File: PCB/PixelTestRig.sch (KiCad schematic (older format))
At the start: 24 parts, among them J1 RPi_GPIO, J2 GS2, P0 STRIP_OUT, P1 STRIP_OUT, P2 STRIP_OUT, P3 STRIP_OUT, P4 STRIP_OUT, P5 STRIP_OUT, P6 APM_INPUT, Q0 IRLB8721PBF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

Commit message: Completed layout
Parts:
- removed PWR2: 1x02, w_conn_mkds:mkds_1,5-2, symbol CONN_01X02
- added R10, R11, R6, R7, R8, R9: 220R, Resistors_THT:R_Axial_DIN0204_L3.6mm_D1.6mm_P5.08mm_Horizontal, symbol R_Small
- Q0, Q1, Q2, Q3, Q4, Q5: footprint (none) -> TO_SOT_Packages_THT:TO-220-3_Vertical
- R0, R1, R2, R3, R4, R5: footprint (none) -> Resistors_THT:R_Axial_DIN0204_L3.6mm_D1.6mm_P5.08mm_Horizontal
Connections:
- net CTL_0: now also R11.1; no longer Q0.1 (G), R0.1
- net CTL_1: now also R10.1; no longer Q1.1 (G), R1.1
- net CTL_2: now also R9.1; no longer Q2.1 (G), R2.1
- net CTL_3: now also R8.1; no longer Q3.1 (G), R3.1
- net CTL_4: now also R7.1; no longer Q4.1 (G), R4.1
- net CTL_5: now also R6.1; no longer Q5.1 (G), R5.1
- new net: Q3.1 (G), R3.1, R9.2
- new net: Q2.1 (G), R2.1, R8.2
- new net: Q5.1 (G), R11.2, R5.1
- new net: Q4.1 (G), R10.2, R4.1
- new net: Q1.1 (G), R1.1, R7.2
- new net: Q0.1 (G), R0.1, R6.2
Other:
- moved on the sheet: J1, J2, P0, P1, P2, P3, P4, P5, P6, PWR1, Q0, Q1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

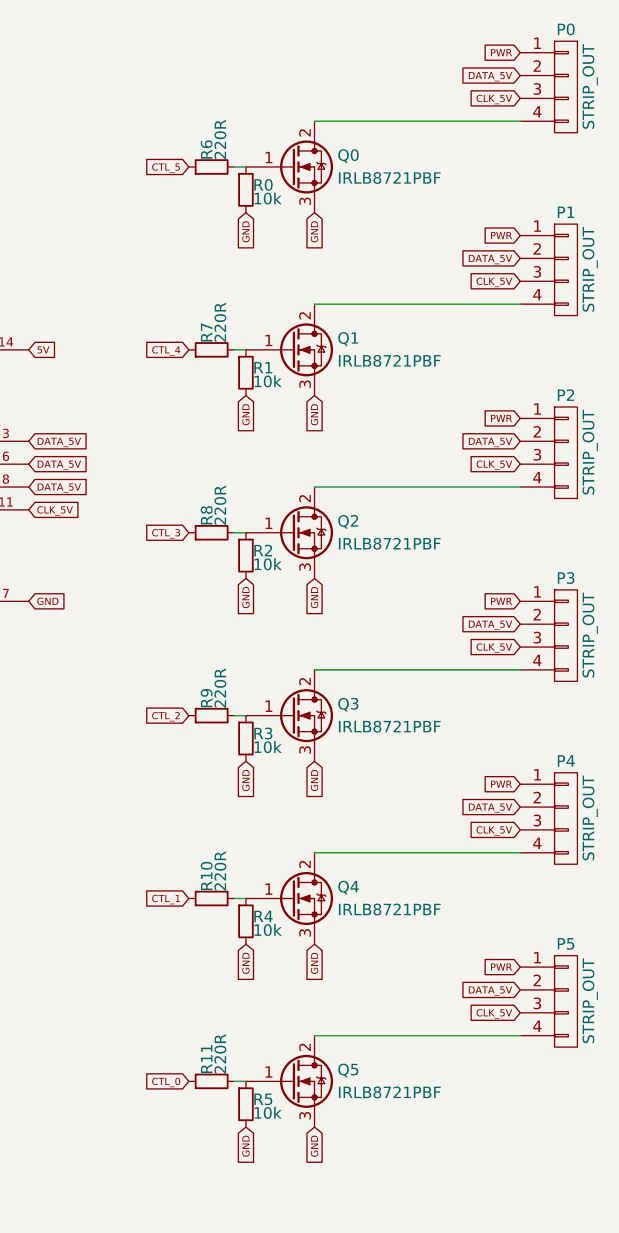
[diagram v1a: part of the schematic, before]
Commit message: Now using PNP transistor
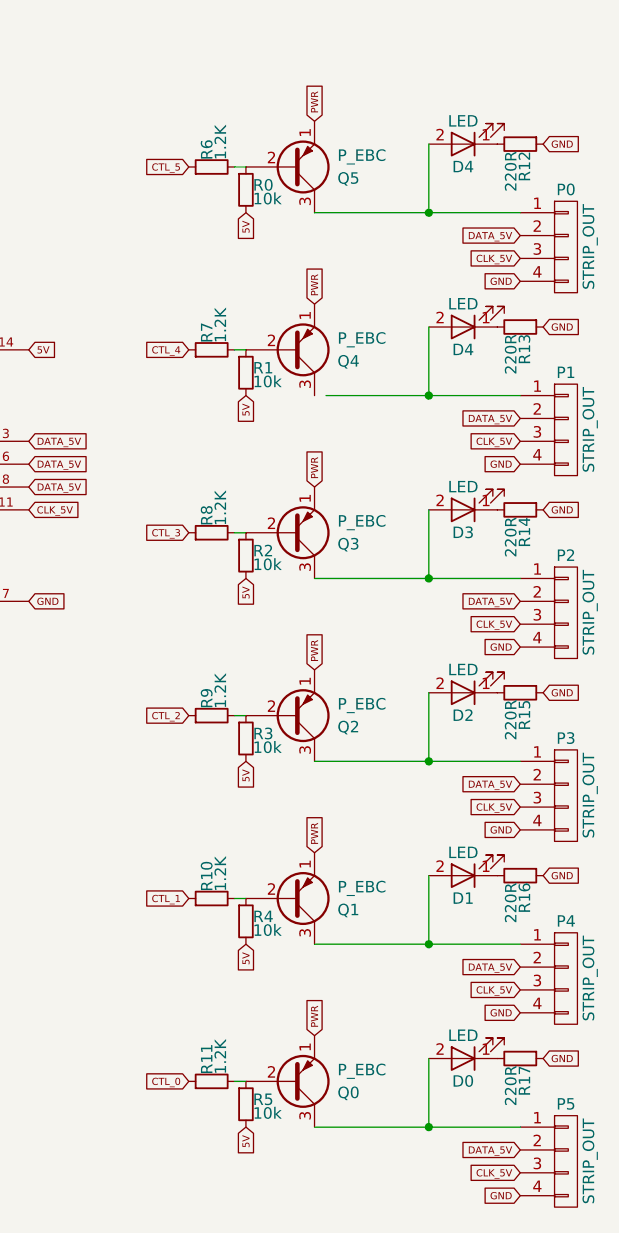
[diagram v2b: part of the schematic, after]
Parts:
- removed Q0, Q1, Q2, Q3, Q4, Q5: IRLB8721PBF, TO_SOT_Packages_THT:TO-220-3_Vertical, symbol Q_NMOS_GDS
- added D0, D1, D2, D3, D4 (x2): LED, symbol LED
- added Q0, Q1, Q2, Q3, Q4, Q5: P_EBC, symbol Q_PNP_EBC
- added R12, R13, R14, R15, R16, R17: 220R, Resistors_THT:R_Axial_DIN0204_L3.6mm_D1.6mm_P5.08mm_Horizontal, symbol R_Small
- R10, R11, R6, R7, R8, R9: value 220R -> 1.2K
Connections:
- net +5V: now also Q0.1 (E), Q1.1 (E), Q2.1 (E), Q3.1 (E), Q4.1 (E), Q5.1 (E); no longer P0.1 (P1), P1.1 (P1), P2.1 (P1), P3.1 (P1), P4.1 (P1), P5.1 (P1)
- net 5V: now also R0.2, R1.2, R2.2, R3.2, R4.2, R5.2
- net GND: now also P0.4 (P4), P1.4 (P4), P2.4 (P4), P3.4 (P4), P4.4 (P4), P5.4 (P4), R12.1, R13.1, R14.1, R15.1, R16.1, R17.1; no longer R0.2, R1.2, R2.2, R3.2, R4.2, R5.2
- net at R3.1, R9.2: now also Q2.2 (B)
- net at R2.1, R8.2: now also Q3.2 (B)
- net at R11.2, R5.1: now also Q0.2 (B)
- net at R10.2, R4.1: now also Q1.2 (B)
- net at R1.1, R7.2: now also Q4.2 (B)
- net at R0.1, R6.2: now also Q5.2 (B)
- new net: D4.2 (A), P0.1 (P1), Q5.3 (C)
- new net: D4.2 (A), P1.1 (P1)
- new net: D3.2 (A), P2.1 (P1), Q3.3 (C)
- new net: D2.2 (A), P3.1 (P1), Q2.3 (C)
- new net: D1.2 (A), P4.1 (P1), Q1.3 (C)
- new net: D0.2 (A), P5.1 (P1), Q0.3 (C)
- new net: D4.1 (K), R12.2
- new net: D4.1 (K), R13.2
- new net: D3.1 (K), R14.2
- new net: D2.1 (K), R15.2
- new net: D1.1 (K), R16.2
- new net: D0.1 (K), R17.2
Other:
- moved on the sheet: P0, P1, P2, P3, P4, P5

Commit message: Updated CvPcb
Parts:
- renumbered D4 to D5
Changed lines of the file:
@@
 	9150 5000 10050 5000
 $Comp
-L LED D4
+L LED D5
 U 1 1 5A5C8FE3
 P 9800 1500
-F 0 "D4" H 9800 1600 50  0000 C CNN
+F 0 "D5" H 9800 1600 50  0000 C CNN
 F 1 "LED" H 9800 1400 50  0000 C CNN
 F 2 "" H 9800 1500 50  0001 C CNN

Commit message: layout redone with PNP
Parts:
- D0, D1, D2, D3, D4, D5: footprint (none) -> LEDs:LED_D3.0mm
- Q0, Q1, Q2, Q3, Q4, Q5: value P_EBC -> PN2907BU; footprint (none) -> TO_SOT_Packages_THT:TO-92_Inline_Narrow_Oval
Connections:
- net at D4.2 (A), P1.1 (P1): now also Q4.3 (C)
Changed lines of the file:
@@
 5V
 $Comp
-L GND #PWR1
+L GND #PWR01
 U 1 1 5A593AA3
 P 2200 3850
-F 0 "#PWR1" H 2200 3600 50  0001 C CNN
+F 0 "#PWR01" H 2200 3600 50  0001 C CNN
 F 1 "GND" H 2200 3700 50  0000 C CNN
 F 2 "" H 2200 3850 50  0001 C CNN
@@
 $EndComp
 $Comp
-L +5V #PWR2
+L +5V #PWR02
 U 1 1 5A593B92
 P 2250 3450
-F 0 "#PWR2" H 2250 3300 50  0001 C CNN
+F 0 "#PWR02" H 2250 3300 50  0001 C CNN
 F 1 "+5V" H 2250 3590 50  0000 C CNN
 F 2 "" H 2250 3450 50  0001 C CNN
@@
 P 9050 1600
 F 0 "Q5" H 9250 1650 50  0000 L CNN
-F 1 "P_EBC" H 9250 1550 50  0000 L CNN
-F 2 "" H 9250 1700 50  0001 C CNN
+F 1 "PN2907BU" H 9250 1550 50  0000 L CNN
+F 2 "TO_SOT_Packages_THT:TO-92_Inline_Narrow_Oval" H 9250 1700 50  0001 C CNN
 F 3 "" H 9050 1600 50  0001 C CNN
 	1    9050 1600
@@
 P 9050 2400
 F 0 "Q4" H 9250 2450 50  0000 L CNN
-F 1 "P_EBC" H 9250 2350 50  0000 L CNN
-F 2 "" H 9250 2500 50  0001 C CNN
+F 1 "PN2907BU" H 9250 2350 50  0000 L CNN
+F 2 "TO_SOT_Packages_THT:TO-92_Inline_Narrow_Oval" H 9250 2500 50  0001 C CNN
 F 3 "" H 9050 2400 50  0001 C CNN
 	1    9050 2400
@@
 P 9050 3200
 F 0 "Q3" H 9250 3250 50  0000 L CNN
-F 1 "P_EBC" H 9250 3150 50  0000 L CNN
-F 2 "" H 9250 3300 50  0001 C CNN
+F 1 "PN2907BU" H 9250 3150 50  0000 L CNN
+F 2 "TO_SOT_Packages_THT:TO-92_Inline_Narrow_Oval" H 9250 3300 50  0001 C CNN
 F 3 "" H 9050 3200 50  0001 C CNN
 	1    9050 3200
@@
 P 9050 4000
 F 0 "Q2" H 9250 4050 50  0000 L CNN
-F 1 "P_EBC" H 9250 3950 50  0000 L CNN
-F 2 "" H 9250 4100 50  0001 C CNN
+F 1 "PN2907BU" H 9250 3950 50  0000 L CNN
+F 2 "TO_SOT_Packages_THT:TO-92_Inline_Narrow_Oval" H 9250 4100 50  0001 C CNN
 F 3 "" H 9050 4000 50  0001 C CNN
 	1    9050 4000
@@
 P 9050 4800
 F 0 "Q1" H 9250 4850 50  0000 L CNN
-F 1 "P_EBC" H 9250 4750 50  0000 L CNN
-F 2 "" H 9250 4900 50  0001 C CNN
+F 1 "PN2907BU" H 9250 4750 50  0000 L CNN
+F 2 "TO_SOT_Packages_THT:TO-92_Inline_Narrow_Oval" H 9250 4900 50  0001 C CNN
 F 3 "" H 9050 4800 50  0001 C CNN
 	1    9050 4800
@@
 P 9050 5600
 F 0 "Q0" H 9250 5650 50  0000 L CNN
-F 1 "P_EBC" H 9250 5550 50  0000 L CNN
-F 2 "" H 9250 5700 50  0001 C CNN
+F 1 "PN2907BU" H 9250 5550 50  0000 L CNN
+F 2 "TO_SOT_Packages_THT:TO-92_Inline_Narrow_Oval" H 9250 5700 50  0001 C CNN
 F 3 "" H 9050 5600 50  0001 C CNN
 	1    9050 5600
@@
 	9150 1800 10050 1800
 Wire Wire Line
-	9200 2600 10050 2600
-Wire Wire Line
 	9150 3400 10050 3400
 Wire Wire Line
@@
 F 0 "D5" H 9800 1600 50  0000 C CNN
 F 1 "LED" H 9800 1400 50  0000 C CNN
-F 2 "" H 9800 1500 50  0001 C CNN
+F 2 "LEDs:LED_D3.0mm" H 9800 1500 50  0001 C CNN
 F 3 "" H 9800 1500 50  0001 C CNN
 	1    9800 1500
@@
 F 0 "D4" H 9800 2400 50  0000 C CNN
 F 1 "LED" H 9800 2200 50  0000 C CNN
-F 2 "" H 9800 2300 50  0001 C CNN
+F 2 "LEDs:LED_D3.0mm" H 9800 2300 50  0001 C CNN
 F 3 "" H 9800 2300 50  0001 C CNN
 	1    9800 2300
@@
 F 0 "D3" H 9800 3200 50  0000 C CNN
 F 1 "LED" H 9800 3000 50  0000 C CNN
-F 2 "" H 9800 3100 50  0001 C CNN
+F 2 "LEDs:LED_D3.0mm" H 9800 3100 50  0001 C CNN
 F 3 "" H 9800 3100 50  0001 C CNN
 	1    9800 3100
@@
 F 0 "D2" H 9800 4000 50  0000 C CNN
 F 1 "LED" H 9800 3800 50  0000 C CNN
-F 2 "" H 9800 3900 50  0001 C CNN
+F 2 "LEDs:LED_D3.0mm" H 9800 3900 50  0001 C CNN
 F 3 "" H 9800 3900 50  0001 C CNN
 	1    9800 3900
@@
 F 0 "D1" H 9800 4800 50  0000 C CNN
 F 1 "LED" H 9800 4600 50  0000 C CNN
-F 2 "" H 9800 4700 50  0001 C CNN
+F 2 "LEDs:LED_D3.0mm" H 9800 4700 50  0001 C CNN
 F 3 "" H 9800 4700 50  0001 C CNN
 	1    9800 4700
@@
 F 0 "D0" H 9800 5600 50  0000 C CNN
 F 1 "LED" H 9800 5400 50  0000 C CNN
-F 2 "" H 9800 5500 50  0001 C CNN
+F 2 "LEDs:LED_D3.0mm" H 9800 5500 50  0001 C CNN
 F 3 "" H 9800 5500 50  0001 C CNN
 	1    9800 5500
@@
 	9650 1500 9650 1800
 Connection ~ 9650 1800
+Wire Wire Line
+	9150 2600 10050 2600
 $EndSCHEMATC
